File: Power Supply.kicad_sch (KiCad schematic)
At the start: 20 parts, among them J1 From Mains, Q1 BC547, U1 AMS1117-3.3, U2 LM2596T-5

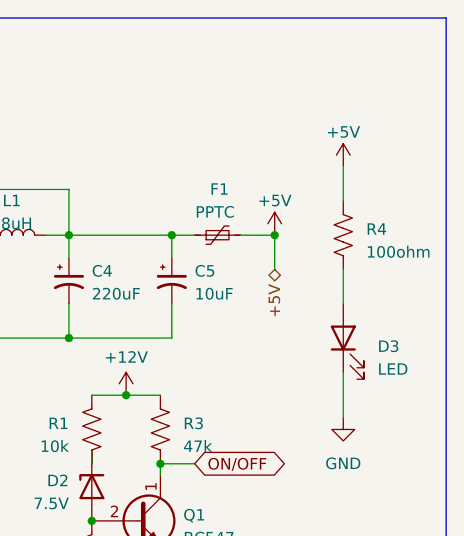
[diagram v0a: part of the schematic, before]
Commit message: "Resolved the issue of SS34 diode footprint. Problem was the pin on the downloaded footprint were not numbered
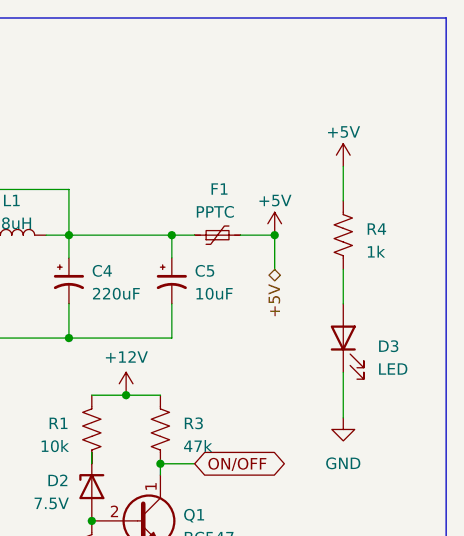
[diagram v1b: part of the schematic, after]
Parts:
- D4, D5: footprint SS34:DIO_SS34 -> KiCad:DIOM8059X256N
- J1: footprint Connector_PinSocket_2.54mm:PinSocket_1x02_P2.54mm_Vertical -> Connector_Phoenix_MSTB:PhoenixContact_MSTBVA_2,5_2-G-5,08_1x02_P5.08mm_Vertical
- R4: value 100ohm -> 1k
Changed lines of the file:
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@@
+    (stroke (width 0) (type default))
+  )
+  (wire (pts (xy 86.36 77.47) (xy 86.36 83.82))
+    (stroke (width 0) (type default))
+  )
+  (wire (pts (xy 110.49 104.14) (xy 116.84 104.14))
+    (stroke (width 0) (type default))
+  )
+  (wire (pts (xy 97.79 72.39) (xy 99.06 72.39))
+    (stroke (width 0) (type default))
+  )
+  (wire (pts (xy 118.11 88.9) (xy 139.7 88.9))
+    (stroke (width 0) (type default))
+  )
+  (wire (pts (xy 154.94 86.36) (xy 154.94 88.9))
+    (stroke (width 0) (type default))
+  )
+  (wire (pts (xy 162.56 77.47) (xy 165.1 77.47))
+    (stroke (width 0) (type default))
+  )
+  (wire (pts (xy 139.7 82.55) (xy 139.7 88.9))
+    (stroke (width 0) (type default))
+  )
+  (polyline (pts (xy 74.93 93.98) (xy 140.97 93.98))
+    (stroke (width 0) (type default))
+  )
+  (wire (pts (xy 175.26 102.87) (xy 179.07 102.87))
+    (stroke (width 0) (type default))
+  )
+  (wire (pts (xy 118.11 72.39) (xy 127 72.39))
+    (stroke (width 0) (type default))
+  )
+  (wire (pts (xy 165.1 72.39) (xy 165.1 77.47))
+    (stroke (width 0) (type default))
+  )
+  (wire (pts (xy 127 77.47) (xy 127 85.09))
     (stroke (width 0) (type default))
   )
   (wire (pts (xy 195.58 69.85) (xy 195.58 73.66))
-    (stroke (width 0) (type default))
-  )
-  (wire (pts (xy 86.36 77.47) (xy 86.36 83.82))
-    (stroke (width 0) (type default))
-  )
-  (wire (pts (xy 110.49 104.14) (xy 116.84 104.14))
-    (stroke (width 0) (type default))
-  )
-  (wire (pts (xy 97.79 72.39) (xy 99.06 72.39))
-    (stroke (width 0) (type default))
-  )
-  (wire (pts (xy 118.11 88.9) (xy 139.7 88.9))
-    (stroke (width 0) (type default))
-  )
-  (wire (pts (xy 154.94 86.36) (xy 154.94 88.9))
-    (stroke (width 0) (type default))
-  )
-  (wire (pts (xy 162.56 77.47) (xy 165.1 77.47))
-    (stroke (width 0) (type default))
-  )
-  (wire (pts (xy 139.7 82.55) (xy 139.7 88.9))
-    (stroke (width 0) (type default))
-  )
-  (polyline (pts (xy 74.93 93.98) (xy 140.97 93.98))
-    (stroke (width 0) (type default))
-  )
-  (wire (pts (xy 175.26 102.87) (xy 179.07 102.87))
-    (stroke (width 0) (type default))
-  )
-  (wire (pts (xy 118.11 72.39) (xy 127 72.39))
-    (stroke (width 0) (type default))
-  )
-  (wire (pts (xy 165.1 72.39) (xy 165.1 77.47))
-    (stroke (width 0) (type default))
-  )
-  (wire (pts (xy 127 77.47) (xy 127 85.09))
     (stroke (width 0) (type default))
   )
@@
       (effects (font (size 1.27 1.27)))
     )
-    (property "Footprint" "SS34:DIO_SS34" (at 154.94 82.55 0)
+    (property "Footprint" "KiCad:DIOM8059X256N" (at 154.94 82.55 0)
       (effects (font (size 1.27 1.27)) hide)
     )
@@
       (effects (font (size 1.27 1.27)) hide)
     )
-    (property "Footprint" "Connector_PinSocket_2.54mm:PinSocket_1x02_P2.54mm_Vertical" (at 81.28 74.93 0)
+    (property "Footprint" "Connector_Phoenix_MSTB:PhoenixContact_MSTBVA_2,5_2-G-5,08_1x02_P5.08mm_Vertical" (at 81.28 74.93 0)
       (effects (font (size 1.27 1.27)) hide)
     )
@@
       (effects (font (size 1.27 1.27)))
     )
-    (property "Footprint" "SS34:DIO_SS34" (at 102.87 72.39 0)
+    (property "Footprint" "KiCad:DIOM8059X256N" (at 102.87 72.39 0)
       (effects (font (size 1.27 1.27)) hide)
     )
@@
       (effects (font (size 1.27 1.27)) (justify left))
     )
-    (property "Value" "100ohm" (at 198.12 79.375 0)
-      (effects (font (size 1.27 1.27)) (justify left))
-    )
+    (property "Value" "1k" (at 198.12 79.375 0)
+      (effects (font (size 1.27 1.27)) (justify left))
+    )
